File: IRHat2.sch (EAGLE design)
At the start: 25 parts, among them T2 2N2907, T3 2N2907

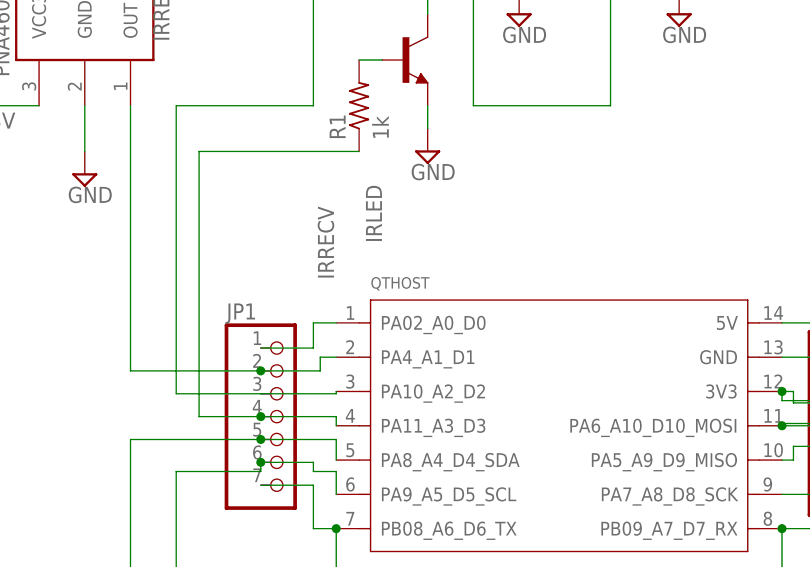
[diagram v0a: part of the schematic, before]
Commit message: tweaks and warning fixes
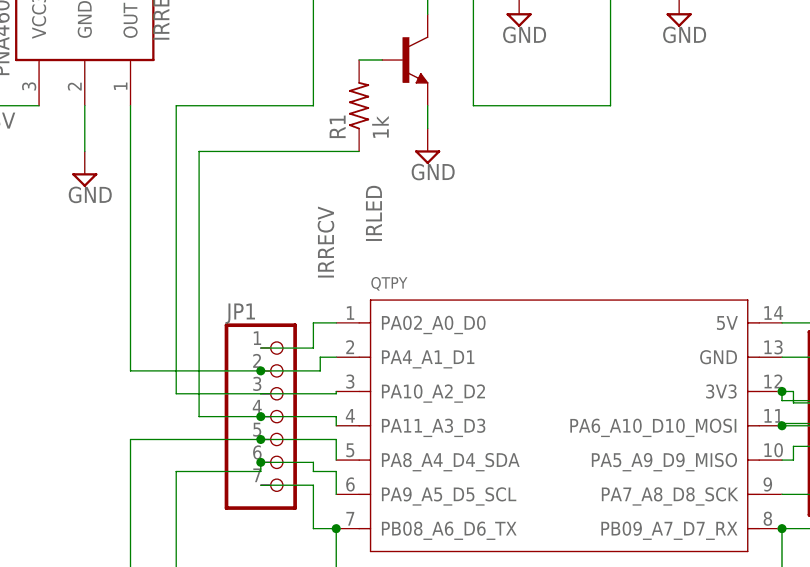
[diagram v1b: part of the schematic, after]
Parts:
- renumbered QTHOST to QTPY
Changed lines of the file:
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@@
 <parts>
 <part name="U$1" library="milador" deviceset="RASPBERRYPI_ZERO" device="" package3d_urn="urn:adsk.eagle:package:9213580/1"/>
-<part name="QTHOST" library="Seeeduino XIAO" deviceset="MOUDLE-SEEEDUINO-XIAO" device=""/>
+<part name="QTPY" library="Seeeduino XIAO" deviceset="MOUDLE-SEEEDUINO-XIAO" device=""/>
 <part name="T1" library="transistor" library_urn="urn:adsk.eagle:library:402" deviceset="*-NPN-" device="TO92-EBC" package3d_urn="urn:adsk.eagle:package:29915/2"/>
 <part name="T2" library="transistor-pnp" library_urn="urn:adsk.eagle:library:399" deviceset="*-?" device="TO92" package3d_urn="urn:adsk.eagle:package:29223/2" technology="MPSA56" value="2N2907"/>
@@
 <attribute name="VALUE" x="228.6" y="122.555" size="1.27" layer="96" font="vector"/>
 </instance>
-<instance part="QTHOST" gate="G$1" x="132.08" y="78.74" smashed="yes">
+<instance part="QTPY" gate="G$1" x="132.08" y="78.74" smashed="yes">
 <attribute name="NAME" x="110.49" y="93.98" size="1.27" layer="95" ratio="12"/>
 <attribute name="VALUE" x="110.49" y="92.71" size="1.27" layer="96" ratio="12"/>
@@
 </segment>
 <segment>
-<pinref part="QTHOST" gate="G$1" pin="GND"/>
+<pinref part="QTPY" gate="G$1" pin="GND"/>
 <wire x1="156.21" y1="86.36" x2="160.02" y2="86.36" width="0.1524" layer="91"/>
 <pinref part="JP2" gate="A" pin="2"/>
@@
 <pinref part="JP1" gate="A" pin="2"/>
 <wire x1="98.298" y1="84.836" x2="104.902" y2="84.836" width="0.1524" layer="91"/>
-<pinref part="QTHOST" gate="G$1" pin="PA4_A1_D1"/>
+<pinref part="QTPY" gate="G$1" pin="PA4_A1_D1"/>
 <wire x1="104.902" y1="84.836" x2="104.902" y2="86.36" width="0.1524" layer="91"/>
 <wire x1="104.902" y1="86.36" x2="106.68" y2="86.36" width="0.1524" layer="91"/>
@@
 <wire x1="91.44" y1="109.22" x2="91.44" y2="79.756" width="0.1524" layer="91"/>
 <pinref part="JP1" gate="A" pin="4"/>
-<pinref part="QTHOST" gate="G$1" pin="PA11_A3_D3"/>
+<pinref part="QTPY" gate="G$1" pin="PA11_A3_D3"/>
 <wire x1="98.298" y1="79.756" x2="106.68" y2="79.756" width="0.1524" layer="91"/>
 <wire x1="106.68" y1="79.756" x2="106.68" y2="78.74" width="0.1524" layer="91"/>
@@
 <wire x1="98.298" y1="87.376" x2="104.14" y2="87.376" width="0.1524" layer="91"/>
 <wire x1="104.14" y1="87.376" x2="104.14" y2="90.17" width="0.1524" layer="91"/>
-<pinref part="QTHOST" gate="G$1" pin="PA02_A0_D0"/>
+<pinref part="QTPY" gate="G$1" pin="PA02_A0_D0"/>
 <wire x1="104.14" y1="90.17" x2="106.68" y2="90.17" width="0.1524" layer="91"/>
 </segment>
@@
 <segment>
 <pinref part="JP1" gate="A" pin="3"/>
-<pinref part="QTHOST" gate="G$1" pin="PA10_A2_D2"/>
+<pinref part="QTPY" gate="G$1" pin="PA10_A2_D2"/>
 <wire x1="98.298" y1="82.296" x2="106.68" y2="82.296" width="0.1524" layer="91"/>
 <wire x1="106.68" y1="82.296" x2="106.68" y2="82.55" width="0.1524" layer="91"/>
@@
 <segment>
 <pinref part="JP1" gate="A" pin="5"/>
-<pinref part="QTHOST" gate="G$1" pin="PA8_A4_D4_SDA"/>
+<pinref part="QTPY" gate="G$1" pin="PA8_A4_D4_SDA"/>
 <wire x1="98.298" y1="77.216" x2="106.68" y2="77.216" width="0.1524" layer="91"/>
 <wire x1="106.68" y1="77.216" x2="106.68" y2="74.93" width="0.1524" layer="91"/>
@@
 <wire x1="104.14" y1="74.676" x2="104.14" y2="73.66" width="0.1524" layer="91"/>
 <wire x1="104.14" y1="73.66" x2="106.68" y2="73.66" width="0.1524" layer="91"/>
-<pinref part="QTHOST" gate="G$1" pin="PA9_A5_D5_SCL"/>
+<pinref part="QTPY" gate="G$1" pin="PA9_A5_D5_SCL"/>
 <wire x1="106.68" y1="73.66" x2="106.68" y2="71.12" width="0.1524" layer="91"/>
 <wire x1="98.298" y1="74.676" x2="98.298" y2="73.66" width="0.1524" layer="91"/>
@@
 <wire x1="98.298" y1="72.136" x2="104.14" y2="72.136" width="0.1524" layer="91"/>
 <wire x1="104.14" y1="72.136" x2="104.14" y2="67.31" width="0.1524" layer="91"/>
-<pinref part="QTHOST" gate="G$1" pin="PB08_A6_D6_TX"/>
+<pinref part="QTPY" gate="G$1" pin="PB08_A6_D6_TX"/>
 <wire x1="104.14" y1="67.31" x2="106.68" y2="67.31" width="0.1524" layer="91"/>
 <pinref part="TXRX" gate="1" pin="1"/>
@@
 <net name="QTMOSI" class="0">
 <segment>
-<pinref part="QTHOST" gate="G$1" pin="PA6_A10_D10_MOSI"/>
+<pinref part="QTPY" gate="G$1" pin="PA6_A10_D10_MOSI"/>
 <pinref part="JP2" gate="A" pin="4"/>
 <wire x1="163.068" y1="78.74" x2="172.72" y2="78.74" width="0.1524" layer="91"/>
@@
 <net name="QTMISO" class="0">
 <segment>
-<pinref part="QTHOST" gate="G$1" pin="PA5_A9_D9_MISO"/>
+<pinref part="QTPY" gate="G$1" pin="PA5_A9_D9_MISO"/>
 <wire x1="156.21" y1="74.93" x2="157.48" y2="74.93" width="0.1524" layer="91"/>
 <wire x1="157.48" y1="74.93" x2="157.48" y2="76.454" width="0.1524" layer="91"/>
@@
 <net name="QTSCK" class="0">
 <segment>
-<pinref part="QTHOST" gate="G$1" pin="PA7_A8_D8_SCK"/>
+<pinref part="QTPY" gate="G$1" pin="PA7_A8_D8_SCK"/>
 <wire x1="156.21" y1="71.12" x2="160.02" y2="71.12" width="0.1524" layer="91"/>
 <wire x1="160.02" y1="71.12" x2="160.02" y2="73.914" width="0.1524" layer="91"/>
@@
 <net name="QTRX" class="0">
 <segment>
-<pinref part="QTHOST" gate="G$1" pin="PB09_A7_D7_RX"/>
+<pinref part="QTPY" gate="G$1" pin="PB09_A7_D7_RX"/>
 <pinref part="JP2" gate="A" pin="7"/>
 <wire x1="156.21" y1="67.31" x2="163.068" y2="67.31" width="0.1524" layer="91"/>
@@
 <net name="3.3V" class="0">
 <segment>
-<pinref part="QTHOST" gate="G$1" pin="3V3"/>
+<pinref part="QTPY" gate="G$1" pin="3V3"/>
 <wire x1="156.21" y1="82.55" x2="157.48" y2="82.55" width="0.1524" layer="91"/>
 <wire x1="157.48" y1="82.55" x2="157.48" y2="81.28" width="0.1524" layer="91"/>
@@
 </segment>
 <segment>
-<pinref part="QTHOST" gate="G$1" pin="5V"/>
+<pinref part="QTPY" gate="G$1" pin="5V"/>
 <pinref part="JP2" gate="A" pin="1"/>
 <wire x1="156.21" y1="90.17" x2="163.068" y2="90.17" width="0.1524" layer="91"/>
